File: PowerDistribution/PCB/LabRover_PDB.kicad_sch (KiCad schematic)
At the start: 0 parts

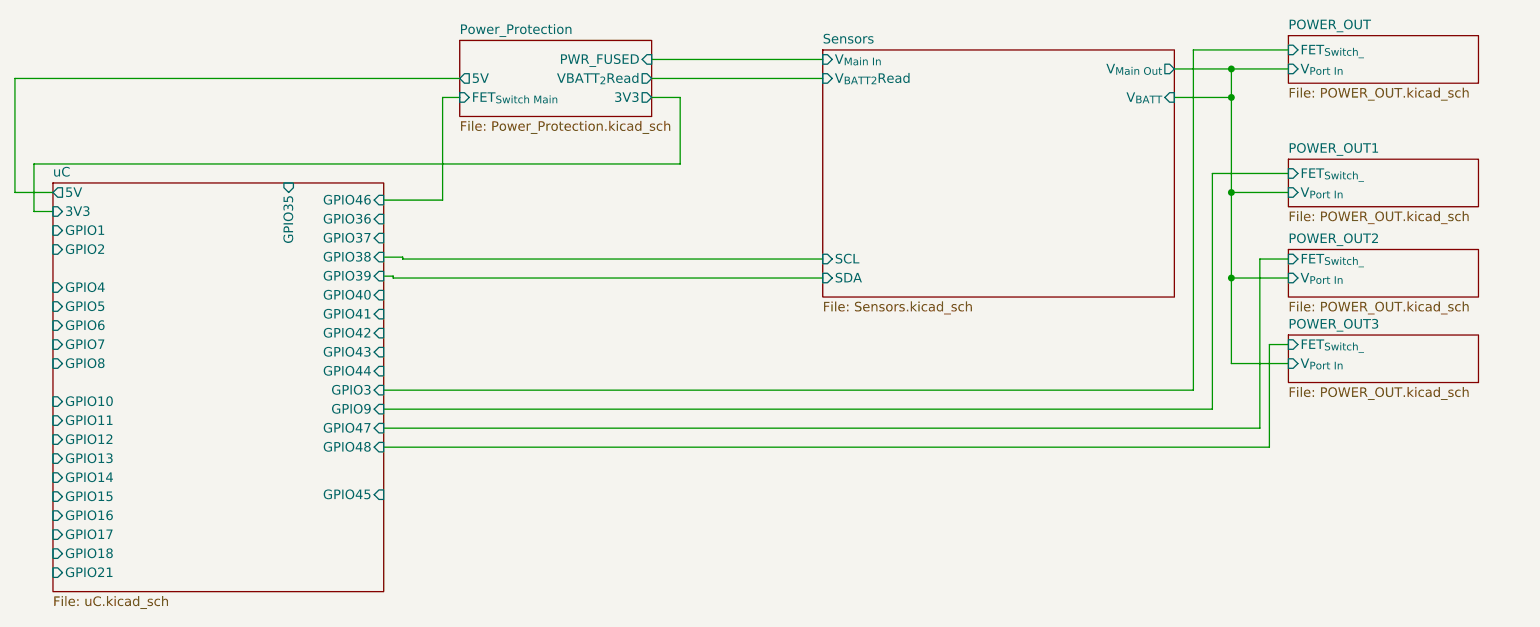
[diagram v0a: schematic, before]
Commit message: Adds PDB v2.0
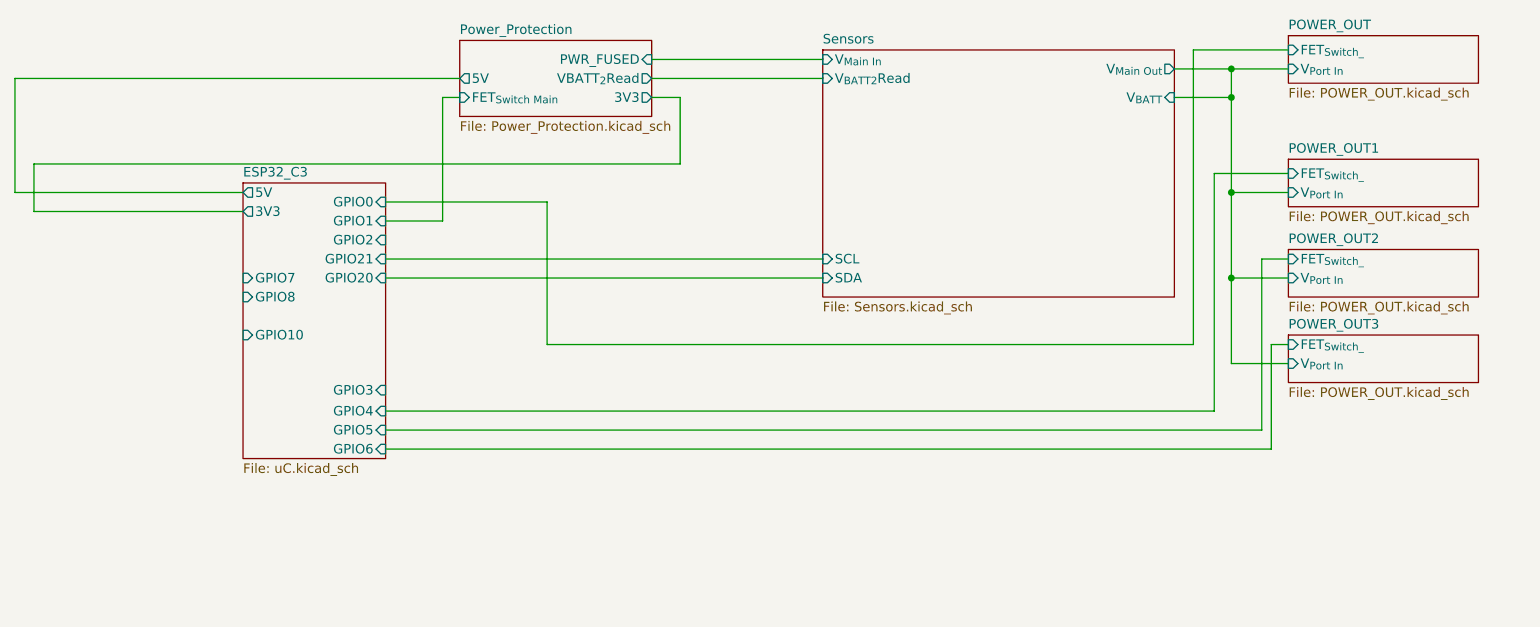
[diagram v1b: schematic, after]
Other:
- sheet uC renamed ESP32_C3
- sheet ESP32_C3 ports: added GPIO0, GPIO20; removed GPIO11, GPIO12, GPIO13, GPIO14, GPIO15, GPIO16, GPIO17, GPIO18, GPIO35, GPIO36, GPIO37, GPIO38, GPIO39, GPIO40, GPIO41, GPIO42, GPIO43, GPIO44, GPIO45, GPIO46, GPIO47, GPIO48, GPIO9
